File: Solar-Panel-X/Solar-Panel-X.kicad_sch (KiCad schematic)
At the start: 73 parts, among them J1 FTS-105-01-L-DV-A, Q1 BSS138DWQ-7, Q2 MBT2222ADW1T1, Q3 BSS138DWQ-7, Q4 MBT2222ADW1T1, U1 BQ25570RGRR, U2 TSL2561

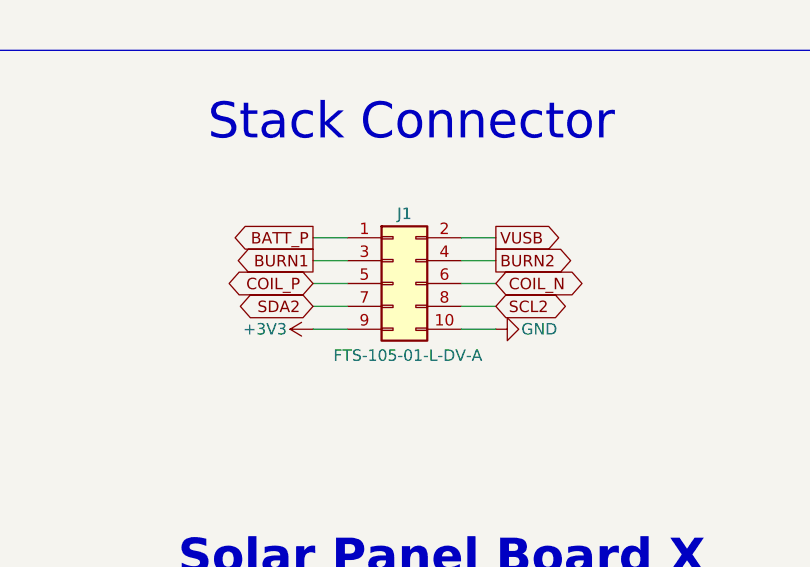
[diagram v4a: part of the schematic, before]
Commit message: Re-check boards, fixed connector pinouts, moved Y+ connector, re-export models
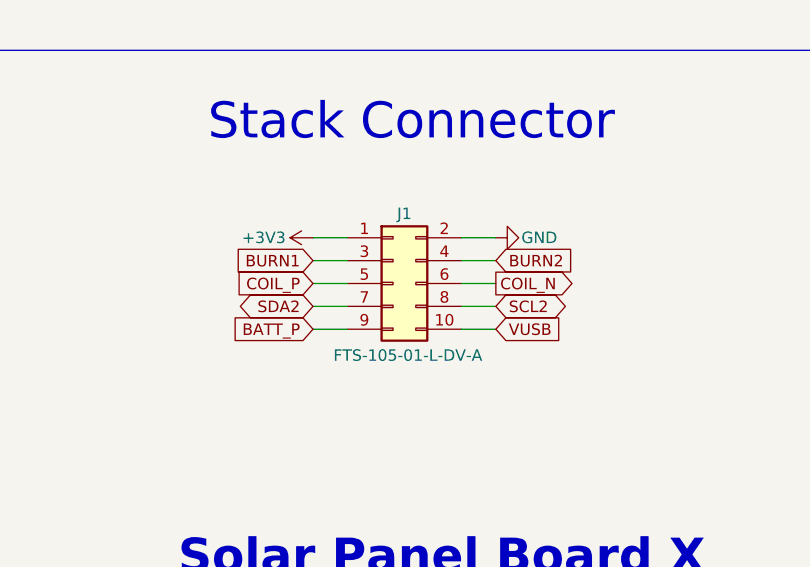
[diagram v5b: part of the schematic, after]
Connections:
- net +3V3: now also J1.1 (Pin_1); no longer J1.9 (Pin_9)
- net BATT_P: now also J1.9 (Pin_9); no longer J1.1 (Pin_1)
- net GND: now also J1.2 (Pin_2); no longer J1.10 (Pin_10)
- net VUSB: now also J1.10 (Pin_10); no longer J1.2 (Pin_2)

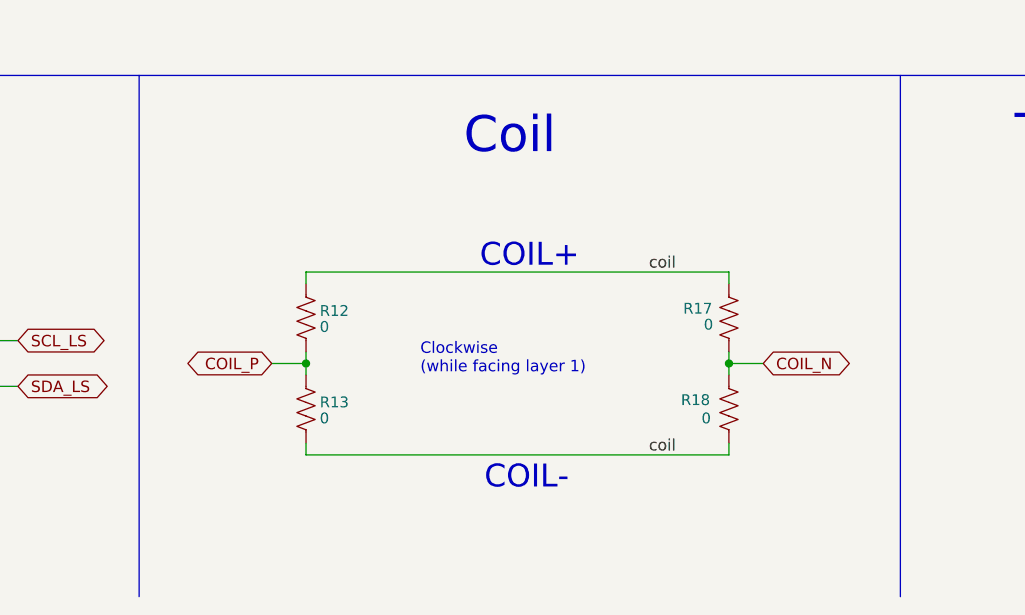
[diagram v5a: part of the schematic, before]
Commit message: Modified coil resistor layout on X board
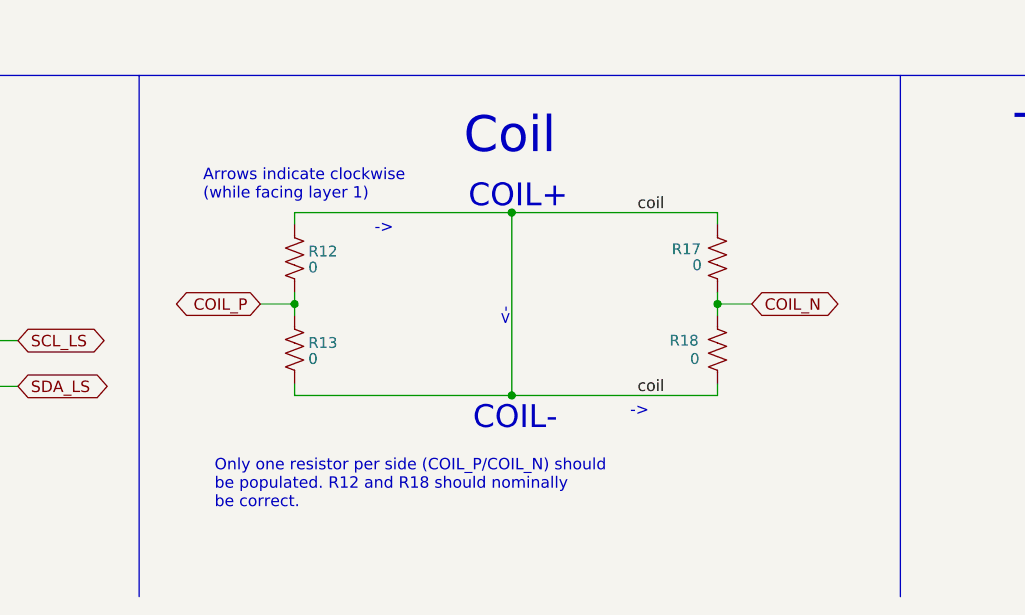
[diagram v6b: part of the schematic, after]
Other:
- note added: "->"
- note added: "<-"
- note added: "Arrows indicate clockwise (while facing layer 1)"
- note added: "Only one resistor per side (COIL_P/COIL_N) should be populated. R12 and R18 should nominally be correct."
- note removed: "Clockwise (while facing layer 1)"
- moved on the sheet: R12, R13, R17, R18
